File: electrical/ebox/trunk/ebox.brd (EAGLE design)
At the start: 127 x 101.6 mm, 158 parts, among them IC1 MAX3221CUE, IC10 SN74LVC1G125, IC11 MAX3221CUE, IC12 INA170, IC13 SN74LVC1G125, IC14 SN74LVC1G125, IC15 MAX3221CUE, IC16 MCP170333MB, IC17 SN74LVC1G125, IC18 SN74LVC1G125, IC19 74ALS04D, IC2 LT3652, IC3 XMEGA128A1, IC4 LT1161, IC5 SN74LVC1G125, IC6 SN74LVC1G125, IC7 MAX3221CUE, IC8 INA170, IC9 SN74LVC1G125, Q1 FDD4141TO252, U1 BLUETOOTH-RN42, U2 D2523T_, X1 7381-3PG-300, X10 DEANS-MALE, X11 B4B-ZR, X12 DEANS-MALE, X13 B4B-ZR, X14 22-23-2021, X15 DEANS-FEMALE, X16 DEANS-FEMALE, X17 USB_A, X2 7381-3PG-300, X3 7381-2PG-300, X4 17984-7PG-300, X5 17984-7PG-300, X6 17984-7PG-300, X7 17984-7PG-300, X8 22-23-2031, X9 22-23-2031

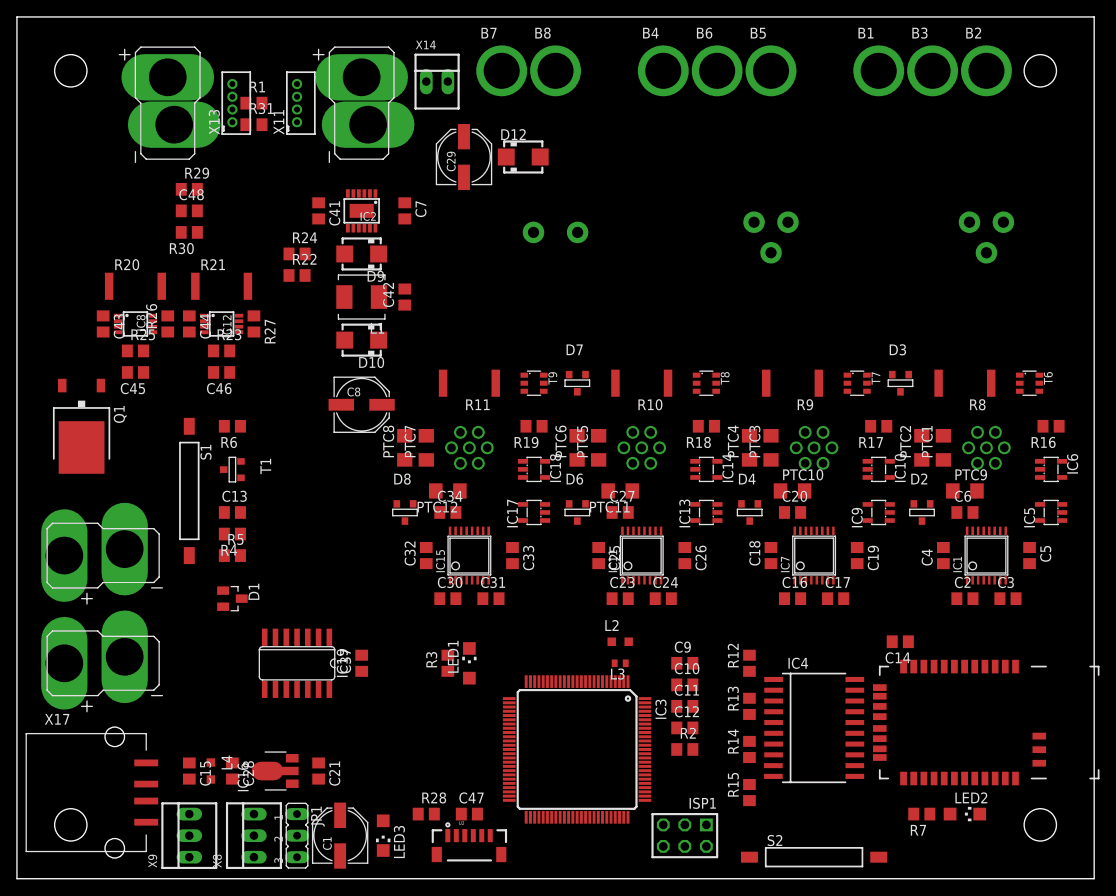
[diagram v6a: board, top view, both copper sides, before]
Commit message: Added rest of routing for much of power section.
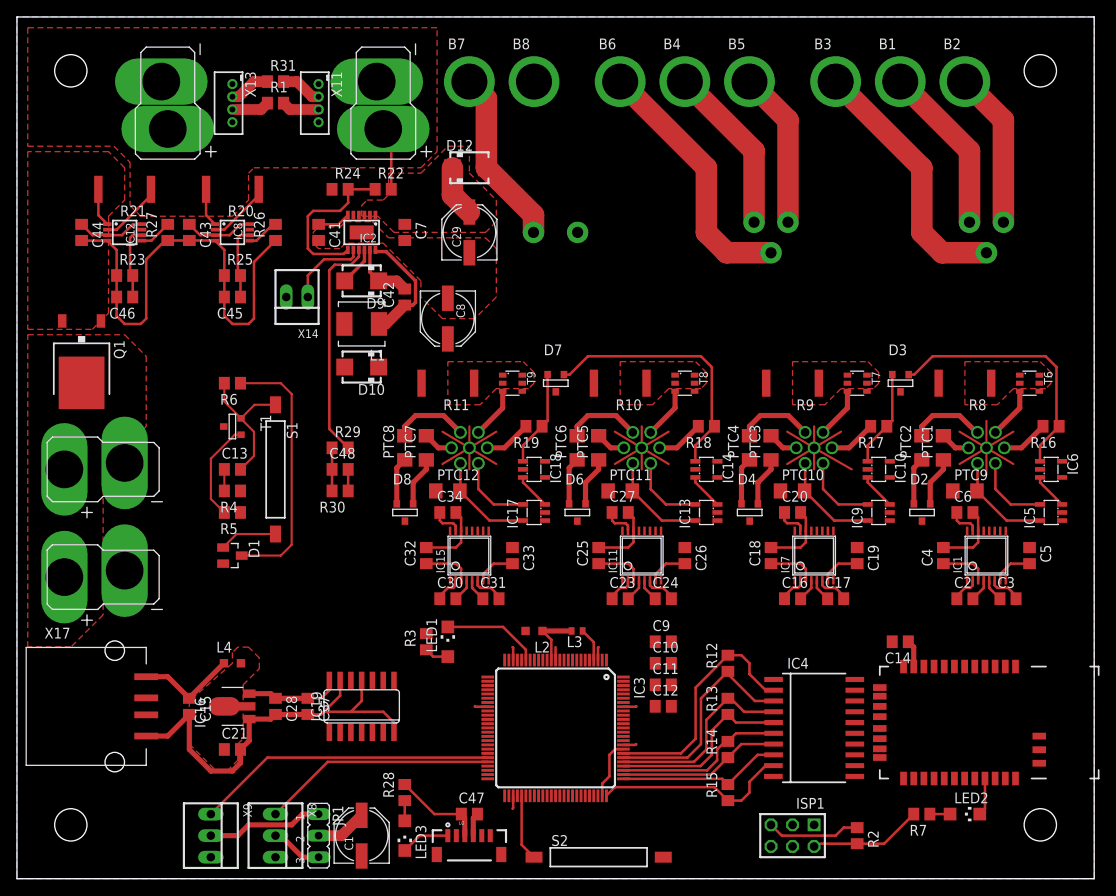
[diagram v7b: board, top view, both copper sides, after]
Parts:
- moved R29 35.3 mm to (38.1, 50.8)
- moved R30 35.3 mm to (38.1, 45.7)
- moved C48 35.3 mm to (38.1, 48.3)
- moved X14 30.3 mm to (33.0, 68.6), turned to 180 degrees
- moved S2 25.4 mm to (68.6, 2.54)
- moved R2 22.7 mm to (99.1, 5.08), turned to 270 degrees
- moved C44 16.7 mm to (7.62, 76.2)
- moved R26 16.7 mm to (30.5, 76.2)
- moved R20 16.2 mm to (25.4, 81.3), turned to 180 degrees
- moved R21 16.2 mm to (12.7, 81.3), turned to 180 degrees
- moved IC12 15.7 mm to (12.7, 76.2)
- moved IC8 15.7 mm to (25.4, 76.2)
- moved C43 14.8 mm to (20.3, 76.2)
- moved R27 14.8 mm to (17.8, 76.2), turned to 90 degrees
- moved R23 14.5 mm to (12.7, 71.1)
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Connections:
- removed net BATT-: X10.NEG, X11.1, X12.NEG, X13.1
- net FAULT1: now also IC3.82; no longer IC3.75
- net FAULT2: now also IC3.80; no longer IC3.77
- net FAULT3: now also IC3.78; no longer IC3.79
- net FAULT4: now also IC3.76; no longer IC3.81
- net GND: now also X10.NEG, X11.1, X12.NEG, X13.1
- net GPIO1A: now also D2.3; no longer D2.2
- net GPIO1B: now also D2.2; no longer D2.3
- net GPIO2A: now also D4.3; no longer D4.2
- net GPIO2B: now also D4.2; no longer D4.3
- net GPIO3A: now also D6.3; no longer D6.2
- net GPIO3B: now also D6.2; no longer D6.3
- net GPIO4A: now also D8.3; no longer D8.2
- net GPIO4B: now also D8.2; no longer D8.3
- net MOT1_SIG: now also IC3.46; no longer IC3.45
- net MOT2_SIG: now also IC3.45; no longer IC3.46
- net PWR_CTL1: now also IC3.81; no longer IC3.76
- net PWR_CTL2: now also IC3.79; no longer IC3.78
- net PWR_CTL3: now also IC3.77; no longer IC3.80
- net PWR_CTL4: now also IC3.75; no longer IC3.82
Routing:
- net GND: track 0.00 -> 245.2 mm
- net +3V3: track 0.00 -> 69.7 mm
- net BATT+: track 0.00 -> 46.4 mm
- net MOT2_SIG: track 0.00 -> 35.4 mm
- net S1_RX_33V: track 0.00 -> 31.0 mm
- net S3_RX_33V: track 0.00 -> 31.0 mm
- net PWR_SENSE: track 0.00 -> 30.8 mm
- net MOT1_C: track 0.00 -> 30.6 mm
- net MOT2_C: track 0.00 -> 30.6 mm
- net FAULT1: track 0.00 -> 28.5 mm
- net MOT1_SIG: track 0.00 -> 27.6 mm
- net PWR_CTL1: track 0.00 -> 26.7 mm
- net FAULT2: track 0.00 -> 23.5 mm
- net PWR_CTL4: track 0.00 -> 23.3 mm
- net PWR_CTL2: track 0.00 -> 22.3 mm
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- added copper zone on layer 1, net +12V
- added copper zone on layer 1, net +5V
- added copper zone on layer 1, net BATT+
- added copper zone on layer 1, net GND
- added copper zone on layer 16, net GND
- added copper zone on layer 1, net N$12
- added copper zone on layer 1, net N$14
- added copper zone on layer 1, net N$15
- added copper zone on layer 1, net N$16
- added copper zone on layer 1, net N$47
- added copper zone on layer 1, net V+

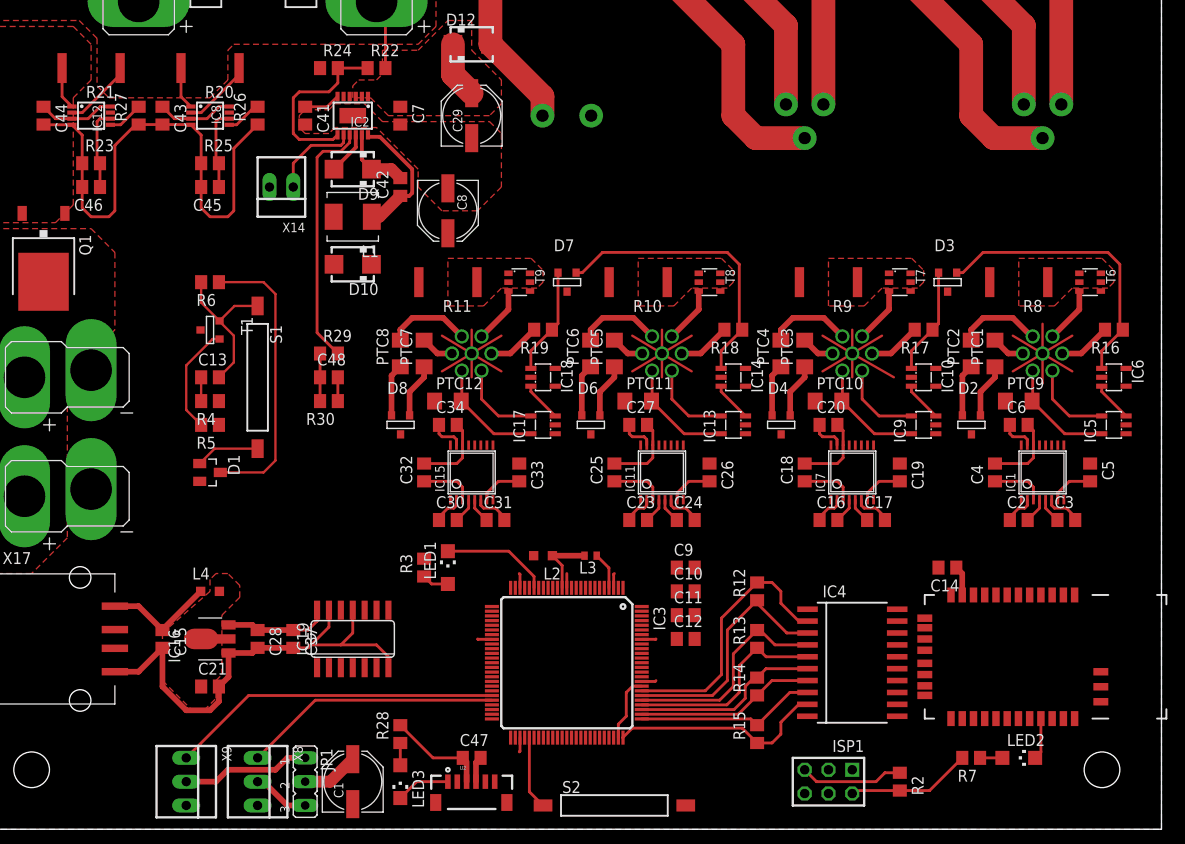
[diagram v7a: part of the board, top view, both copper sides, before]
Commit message: Loads better routing of power.
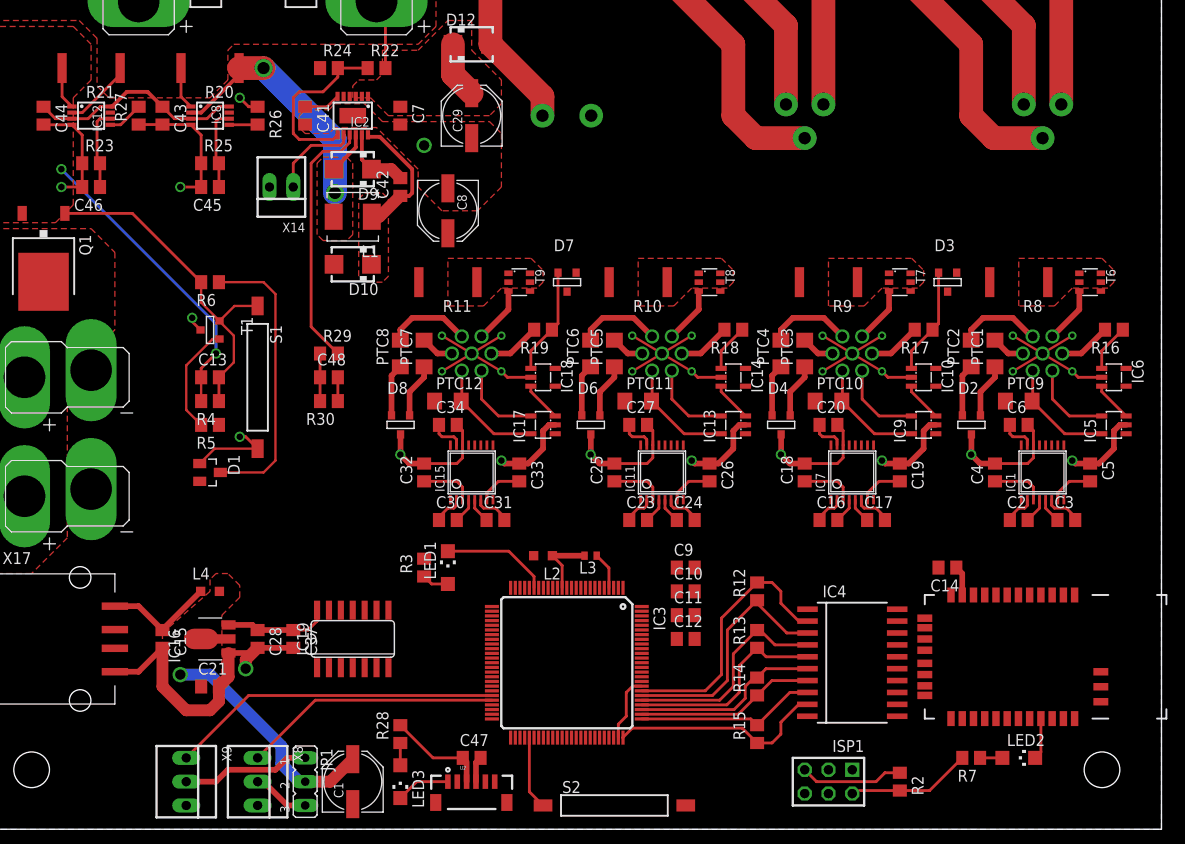
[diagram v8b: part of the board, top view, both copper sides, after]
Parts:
- turned R26 to 270 degrees
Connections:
- net +5V: now also IC16.2
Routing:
- net V+: track 7.08 -> 36.8 mm, vias 0 -> 2
- net S1_RX_33V: track 31.0 -> 5.06 mm
- net S3_RX_33V: track 31.0 -> 5.06 mm
- net N$13: track 17.0 -> 37.1 mm
- net +5V: track 6.07 -> 25.3 mm, vias 0 -> 1
- net CHRG+: track 12.2 -> 31.3 mm, vias 0 -> 2
- net +3V3: track 69.7 -> 76.6 mm
- net GND: track 245.2 -> 239.6 mm, vias 0 -> 31
- net N$48: track 3.83 -> 3.04 mm
- net BATT+: track 46.4 -> 46.9 mm
- added copper zone on layer 1, net CHRG+
- added copper zone on layer 1, net N$42
